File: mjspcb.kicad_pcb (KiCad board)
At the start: 2 copper layers, 97.2 x 55.9 mm, 78 parts, among them P1 Batteries, P10 Lipo, P2 serial breakout, P3 I2C breakout, P4 GPS, P5 piezo, P6 BPW34, P7 electrodes, P8 perfboard breakout, P9 reset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

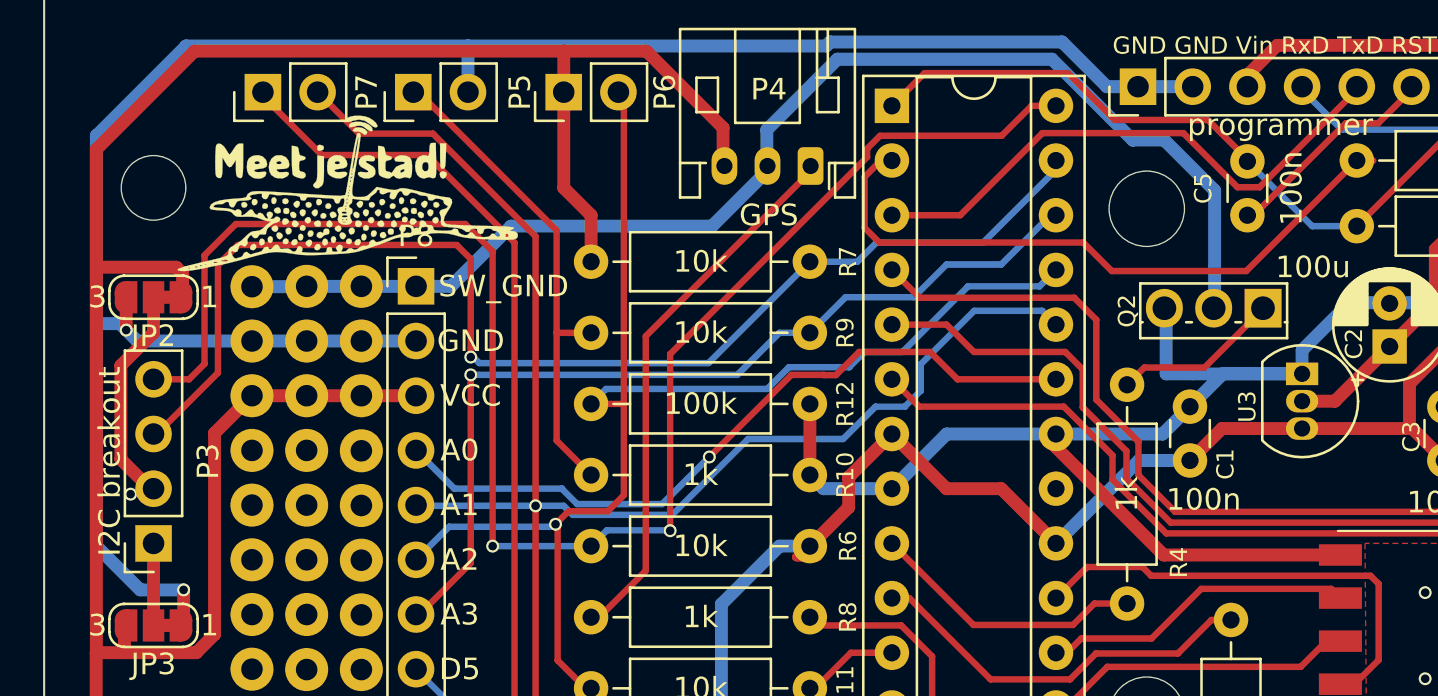
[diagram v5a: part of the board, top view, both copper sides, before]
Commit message: Run a track & via cleanup
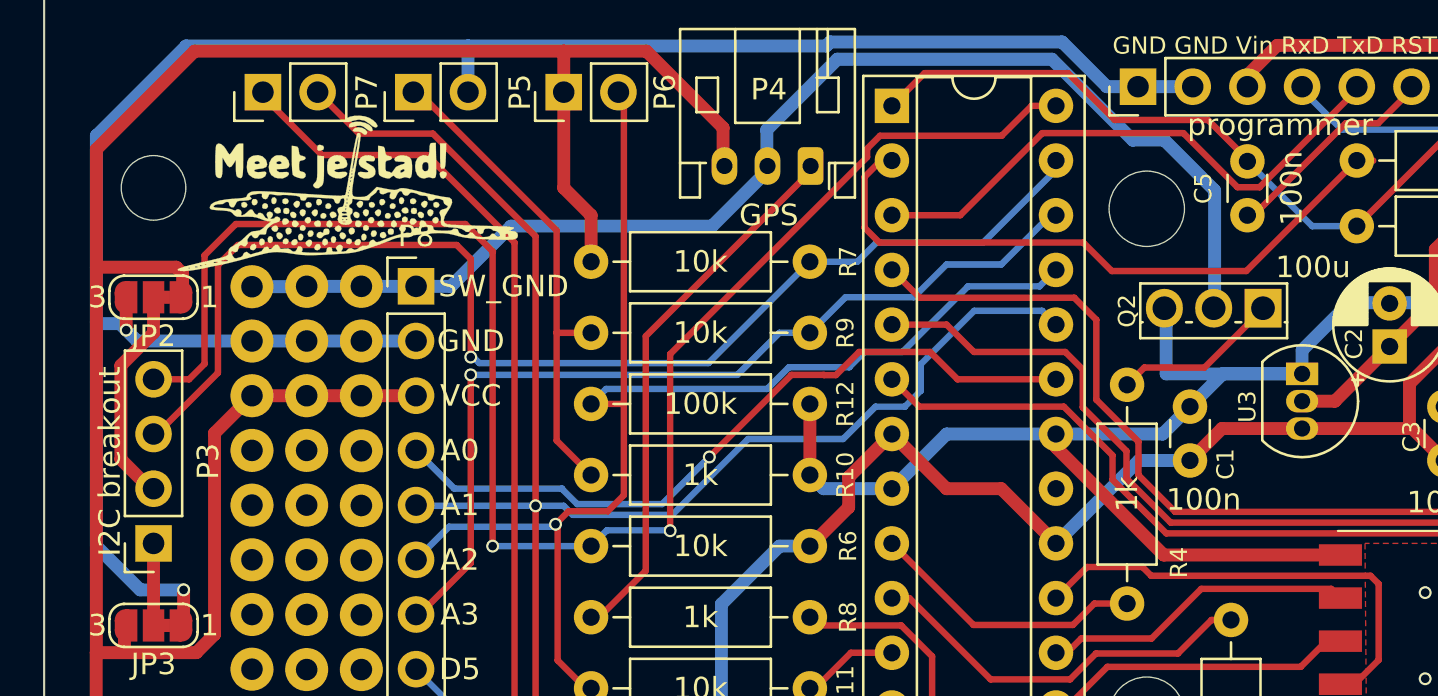
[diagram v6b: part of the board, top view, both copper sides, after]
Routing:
- net VCC: track 232.8 -> 232.2 mm
- net (no net): vias 1 -> 0

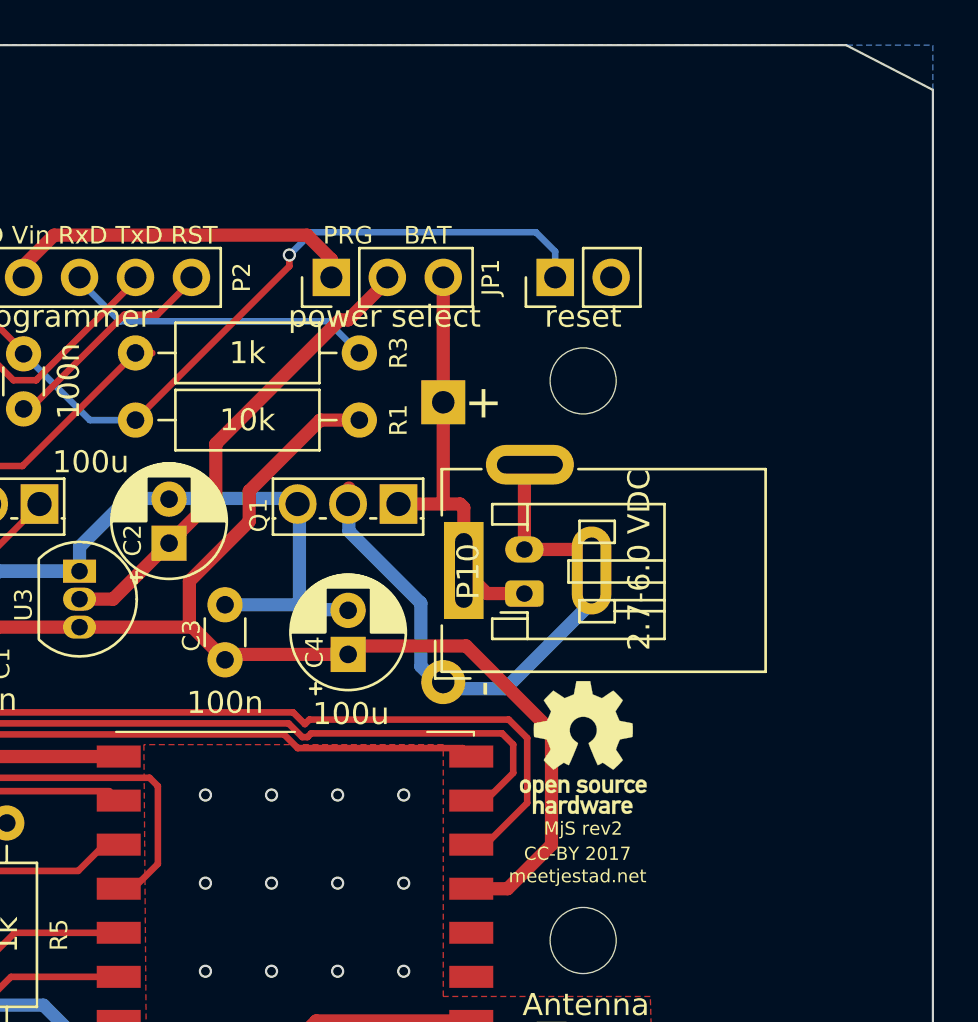
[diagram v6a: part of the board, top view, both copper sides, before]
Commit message: Add slot for GPS
This also moves the barrel jack and LiPo connectors to make room for the
slot, and removes some of the ground plane to prevent interfering with
the GPS and LoRa antenna.
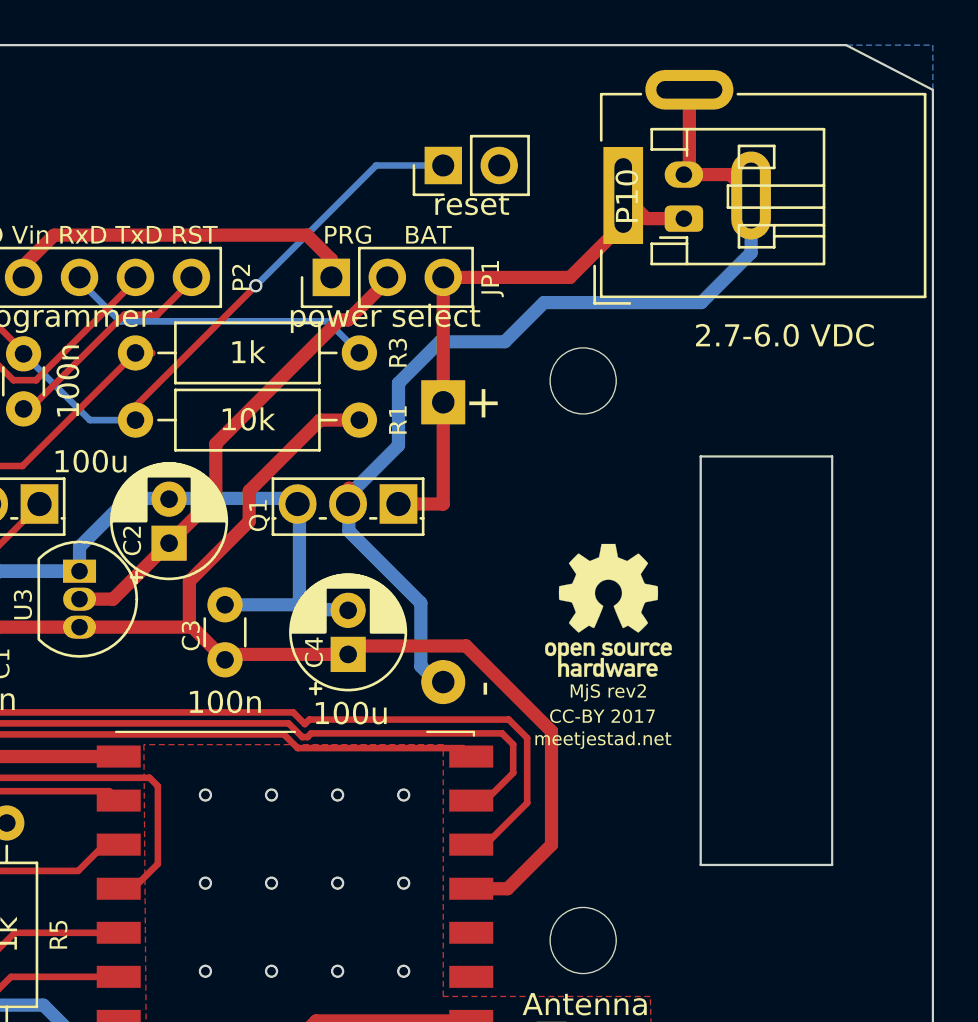
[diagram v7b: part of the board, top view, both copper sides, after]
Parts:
- moved DC1 18.5 mm to (217.7, 99.5)
- moved P10 18.5 mm to (220.5, 100.6)
- moved P9 7.18 mm to (209.6, 98.2)
- moved LOGO1 6.33 mm to (217.0, 118.4)
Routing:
- net -BATT: track 31.5 -> 46.5 mm
- net +BATT: track 21.0 -> 26.4 mm
- net RST: track 49.9 -> 44.6 mm
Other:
- outline, holes or cut-outs redrawn

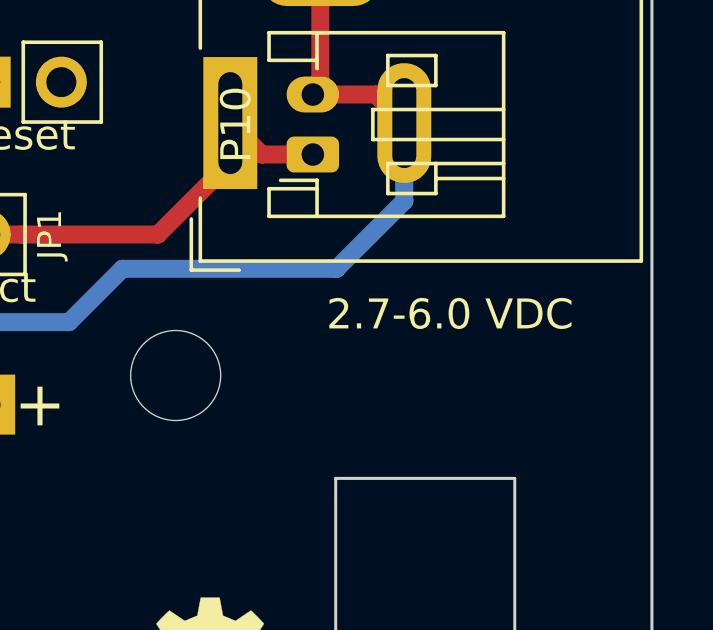
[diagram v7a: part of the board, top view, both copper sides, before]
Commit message: Fix input voltage range on silkscreen
This changes the minimum to 3.6V, which should be safe. The MCP1700
datasheet has a dropout voltage of 178mV typical, 350mV max (at 250mA).
Given we need a lower current, calculating with a 300mV dropout seems
ok.
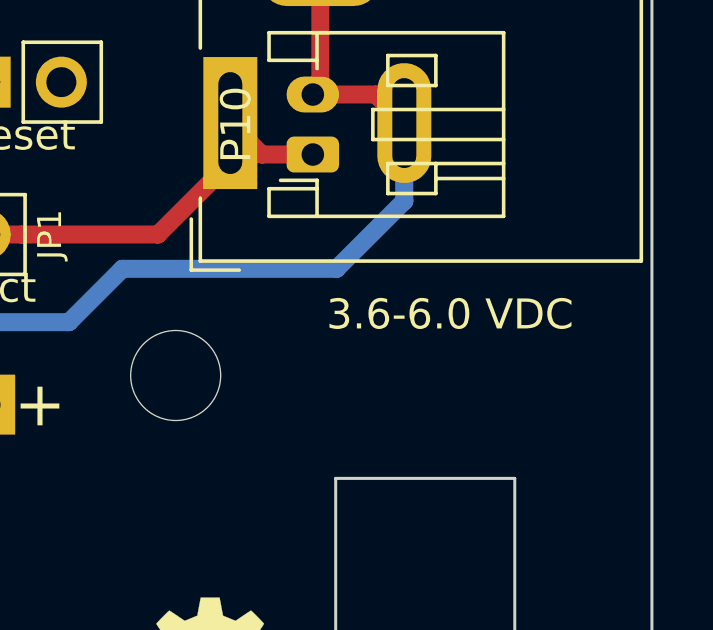
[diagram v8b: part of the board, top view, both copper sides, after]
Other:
- board text added: "3.6-6.0 VDC"
- board text removed: "2.7-6.0 VDC"
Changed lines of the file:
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@@
     (effects (font (size 1 1) (thickness 0.15)))
   )
-  (gr_text "2.7-6.0 VDC" (at 225.044 105.918) (layer F.SilkS)
+  (gr_text "3.6-6.0 VDC" (at 225.044 105.918) (layer F.SilkS)
     (effects (font (size 1 1) (thickness 0.25)))
   )
